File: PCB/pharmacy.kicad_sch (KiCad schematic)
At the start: 13 parts, among them J1 PWR_Conn, SW1 next_Button, U1 ctrlr_TL, U2 LEDs_T, U3 ctrlr_BR, U4 LEDs_B, U5 LEDs_R, U6 LEDs_L, U7 ctrlr_C, U8 ESP32-C6-DEVKITC-1-N8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

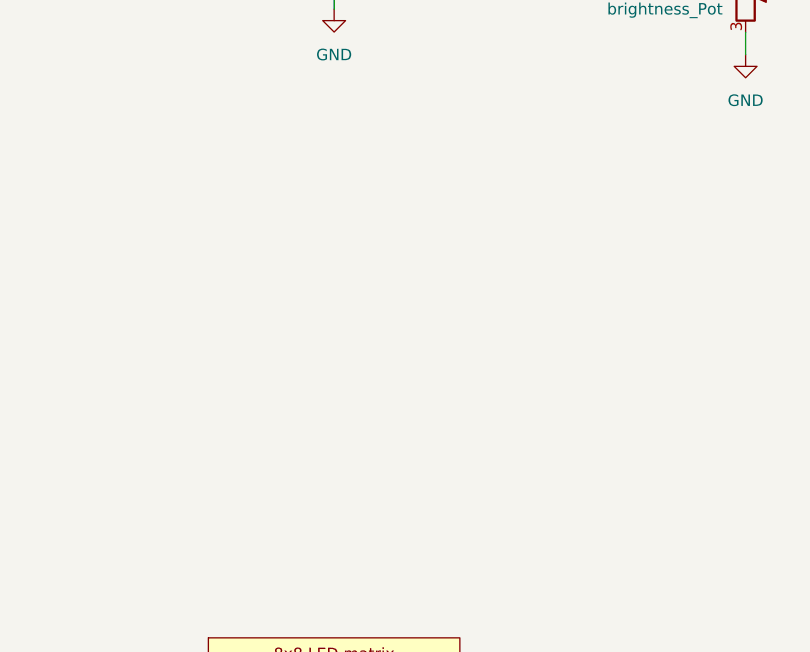
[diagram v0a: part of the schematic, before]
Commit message: Added mounting holes to PCB
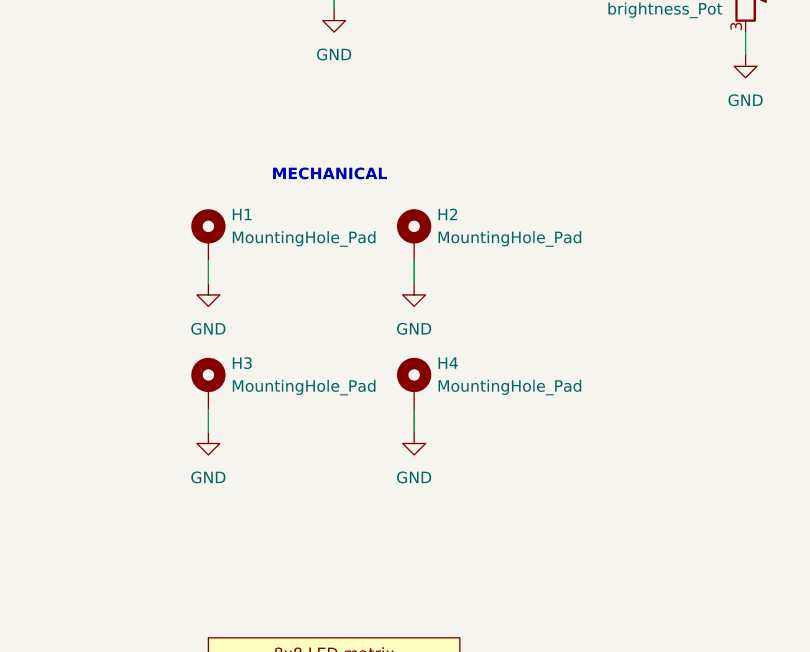
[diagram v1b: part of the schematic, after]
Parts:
- added H1, H2, H3, H4: MountingHole_Pad, MountingHole:MountingHole_2.7mm_M2.5_ISO7380_Pad, symbol Mechanical:MountingHole_Pad
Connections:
- net GND: now also H1.1, H2.1, H3.1, H4.1
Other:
- note added: "MECHANICAL"
